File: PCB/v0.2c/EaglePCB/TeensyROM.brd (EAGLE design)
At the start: 61 x 68.6 mm, 25 parts, among them J1 C64-EXPANSION-PORT, J2 292303-1, J3 J1B1211CCD, J4 3 pin Header, U1 TEENSY41, U2 74LCV245, U3 74LCV245, U4 74LCV245, U5 74LCV245, U6 74LVC07

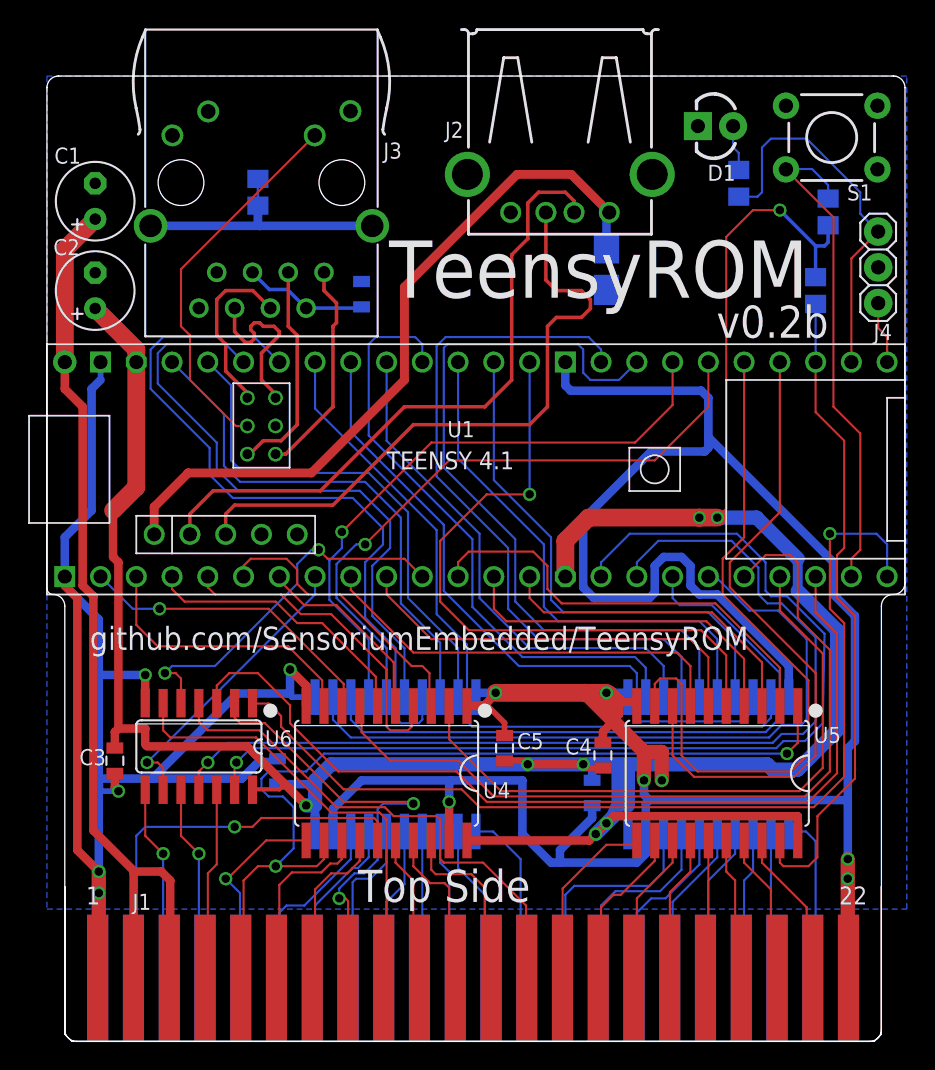
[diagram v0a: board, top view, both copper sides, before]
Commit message: v0.2c PCB released v0.2b archived PCB_History updated
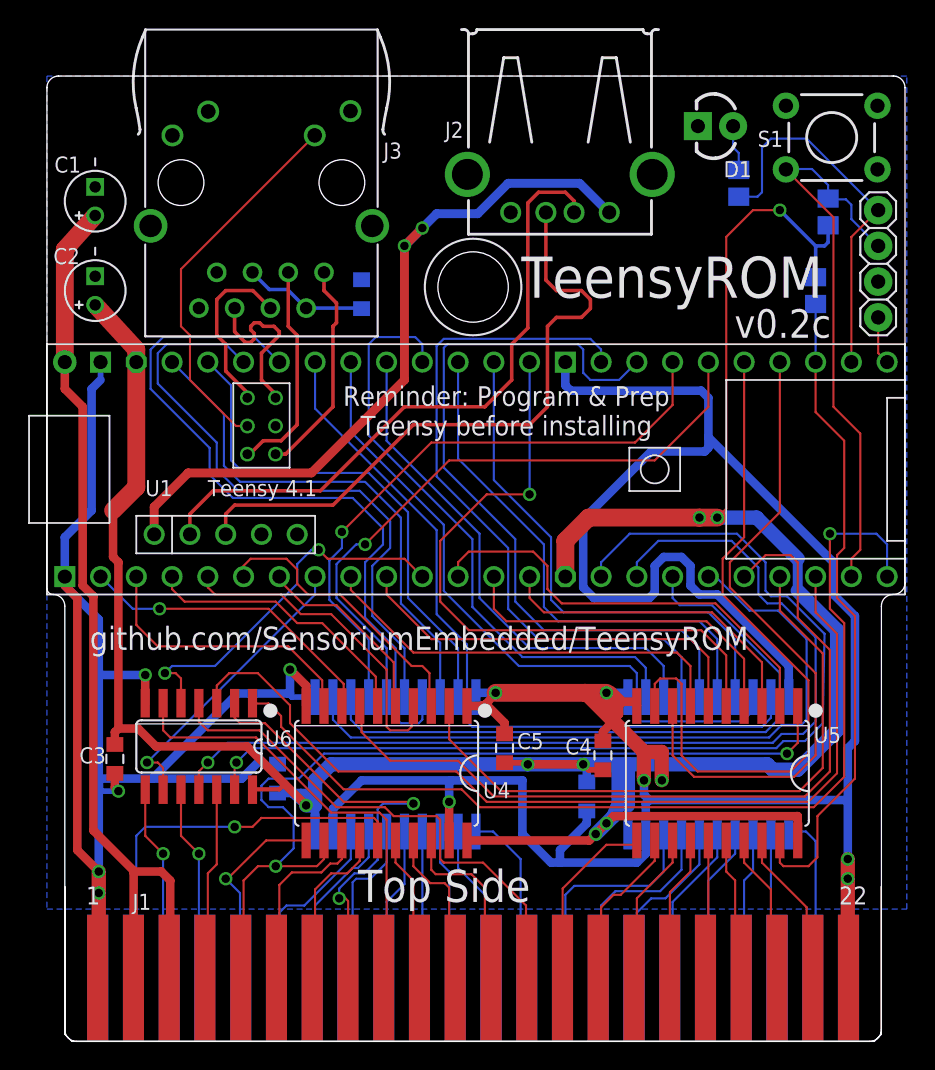
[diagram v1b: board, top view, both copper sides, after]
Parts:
- removed C9: 100uF, rcl:A/3216-18W
- removed JP1: SHORTSMT, TeensyROM:SHORT
- added U$1: (no value), TeensyROM_phys:3,0
- C1, C2: device rcl:E2,5-6 -> TeensyROM:E2-4
- C4, C6, C7, C8: device cap:0805 -> TeensyROM:0805
- J4: value 3 pin Header -> 4 pin header; device TeensyROM:1X03 -> pinhead:1X04
- U1: value TEENSY41 -> Teensy 4.1
- moved C7 0.51 mm to (15.1, 18.7)
- moved C6 0.46 mm to (37.1, 17.4)
- moved J4 0.25 mm to (57.8, 55.2)
- moved C3 0.13 mm to (3.56, 20.1)
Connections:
- removed net ETH_SH: J3.S1, J3.S2, JP1.2
- net !BUTTON: now also J4.3
- net GND: now also J3.S1, J3.S2; no longer C9.-, JP1.1
- net LED: now also J4.4; no longer J4.3
- net VHST: no longer C9.+
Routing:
- net ETH_SH: track 17.2 -> 0.00 mm
- net !BUTTON: track 35.8 -> 41.4 mm
- net GND: track 328.9 -> 326.8 mm
- net +3V3: track 212.1 -> 214.1 mm
- net DEBUG: track 4.45 -> 3.44 mm
- net VHST: track 51.7 -> 52.0 mm, vias 0 -> 2
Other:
- board text added: "Reminder: Program & Prep Teensy before installing"
- board text added: "Serial Num:"
- board text added: "v0.2c"
- board text removed: "v0.2b"

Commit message: Corrected schematic value of 74LVC245, was listed as 74LCV245
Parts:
- U2, U3, U4, U5: value 74LCV245 -> 74LVC245
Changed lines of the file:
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@@
 <attribute name="VALUE" x="4.826" y="56.007" size="1.27" layer="27" ratio="10" rot="R90"/>
 </element>
-<element name="U4" library="TeensyROM" package="SO20W" value="74LCV245" x="22.86" y="19.05" smashed="yes" rot="R180">
+<element name="U4" library="TeensyROM" package="SO20W" value="74LVC245" x="22.86" y="19.05" smashed="yes" rot="R180">
 <attribute name="VALUE" x="26.67" y="20.828" size="1.27" layer="27" ratio="10" rot="R180"/>
 <attribute name="NAME" x="29.718" y="17.272" size="1.143" layer="25" font="vector" ratio="10"/>
 </element>
-<element name="U2" library="TeensyROM" package="SO20W" value="74LCV245" x="45.72" y="19.685" smashed="yes" rot="MR180">
+<element name="U2" library="TeensyROM" package="SO20W" value="74LVC245" x="45.72" y="19.685" smashed="yes" rot="MR180">
 <attribute name="VALUE" x="41.91" y="21.463" size="1.27" layer="28" ratio="10" rot="MR180"/>
 <attribute name="NAME" x="38.735" y="22.0218" size="1.143" layer="26" font="vector" ratio="10" rot="MR0"/>
 </element>
-<element name="U3" library="TeensyROM" package="SO20W" value="74LCV245" x="23.495" y="19.685" smashed="yes" rot="MR180">
+<element name="U3" library="TeensyROM" package="SO20W" value="74LVC245" x="23.495" y="19.685" smashed="yes" rot="MR180">
 <attribute name="VALUE" x="19.685" y="21.463" size="1.27" layer="28" ratio="10" rot="MR180"/>
 <attribute name="NAME" x="16.6116" y="21.8694" size="1.143" layer="26" font="vector" ratio="10" rot="MR0"/>
 </element>
-<element name="U5" library="TeensyROM" package="SO20W" value="74LCV245" x="46.355" y="19.05" smashed="yes" rot="R180">
+<element name="U5" library="TeensyROM" package="SO20W" value="74LVC245" x="46.355" y="19.05" smashed="yes" rot="R180">
 <attribute name="VALUE" x="50.165" y="20.828" size="1.27" layer="27" ratio="10" rot="R180"/>
 <attribute name="NAME" x="53.213" y="21.209" size="1.143" layer="25" font="vector" ratio="10"/>
